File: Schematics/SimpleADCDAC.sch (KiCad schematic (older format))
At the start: 83 parts, among them CN701 COAX, CN702 COAX, P701 CONN_02X05, P702 CONN_2x1, P703 CONN_02X05, P704 CONN_3x1, P705 CONN_3x1, U701 IC-REG-LM317-TO220, U702 IC-DAC-WM8501, U703 IC-ADC-WM8783, U704 IC-REG-XC6210B332MR

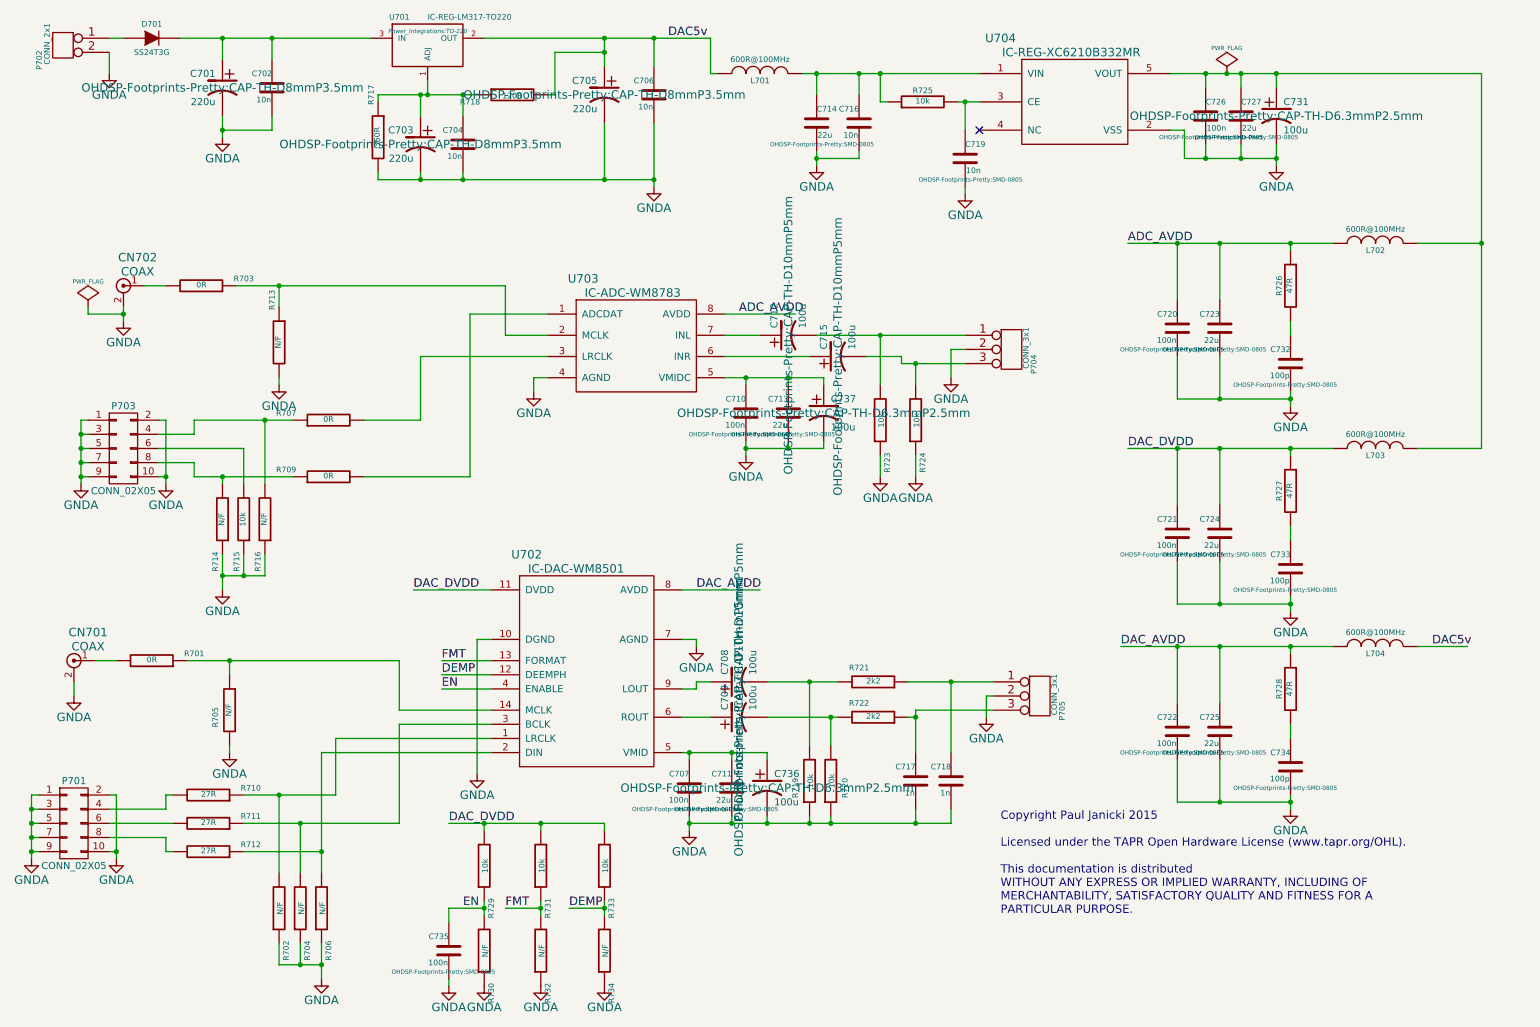
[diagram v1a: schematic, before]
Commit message: WIP
Add master audio clock to I2S headers.
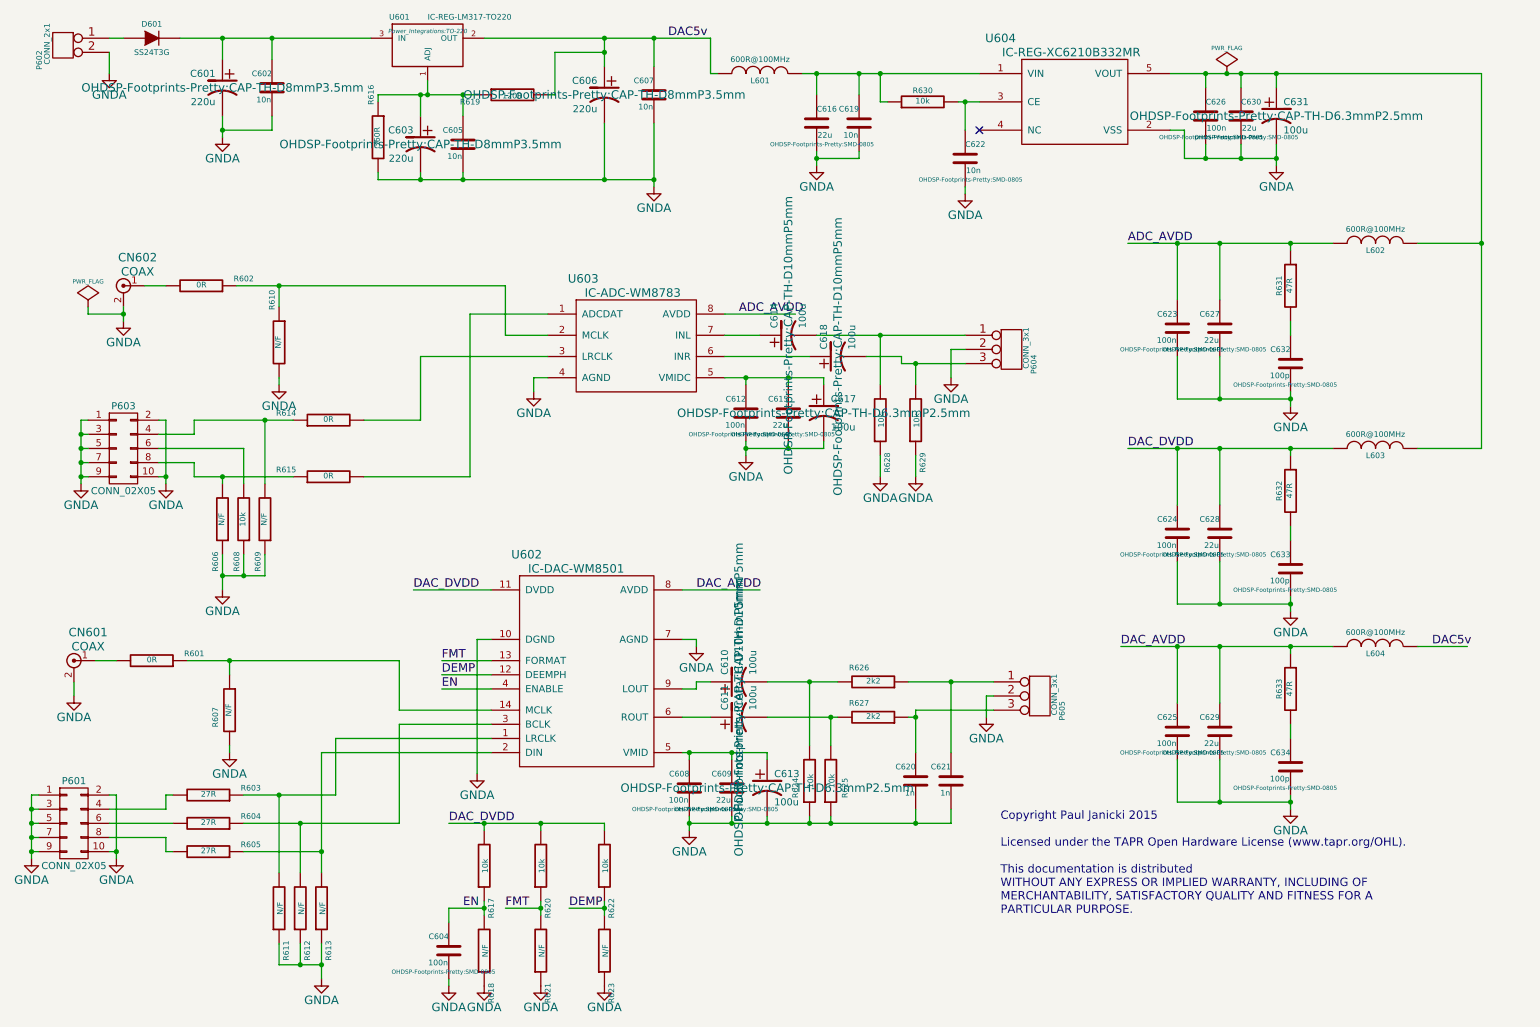
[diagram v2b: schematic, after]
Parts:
- renumbered C701 to C601, C702 to C602, C703 to C603, C735 to C604, C704 to C605, C705 to C606, C706 to C607, C707 to C608, C711 to C609, C708 to C610, C709 to C611, C710 to C612, C736 to C613, C712 to C614, C713 to C615, C714 to C616, C737 to C617, C715 to C618, C716 to C619, C717 to C620, C718 to C621, C719 to C622, C720 to C623, C721 to C624, C722 to C625, C726 to C626, C723 to C627, C724 to C628, C725 to C629, C727 to C630, C731 to C631, C732 to C632, C733 to C633, C734 to C634, CN701 to CN601, CN702 to CN602, D701 to D601, L701 to L601, L702 to L602, L703 to L603, L704 to L604, P701 to P601, P702 to P602, P703 to P603, P704 to P604, P705 to P605, R701 to R601, R703 to R602, R710 to R603, R711 to R604, R712 to R605, R714 to R606, R705 to R607, R715 to R608, R716 to R609, R713 to R610, R702 to R611, R704 to R612, R706 to R613, R707 to R614, R709 to R615, R717 to R616, R729 to R617, R730 to R618, R718 to R619, R731 to R620, R732 to R621, R733 to R622, R734 to R623, R719 to R624, R720 to R625, R721 to R626, R722 to R627, R723 to R628, R724 to R629, R725 to R630, R726 to R631, R727 to R632, R728 to R633, U701 to U601, U702 to U602, U703 to U603, U704 to U604
